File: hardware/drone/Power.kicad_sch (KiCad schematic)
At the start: 96 parts, among them Q1 ISP650P06NM, U1 STM32N645I0, U13 LP5907, U16 LMR51635XFDDCR, U18 TPS2121, U3 TPS628303, U4 TPS7A2118PQWDSGRQ1, U5 TPS628303

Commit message: More footprints
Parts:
- removed C97: 10u, symbol Device:C
- added C114: 2.2u, Capacitor_SMD:C_1206_3216Metric, symbol Device:C
- added C125: 100n, Capacitor_SMD:C_0603_1608Metric, symbol Device:C
- added C126: 22u, Capacitor_SMD:CP_Elec_6.3x5.4, symbol Device:C
- added R45: 2R, Resistor_SMD:R_0402_1005Metric, symbol Device:R
- C10, C100, C101, C102, C103, C104, C105, C106, C107, C108, C109, C110, C111, C112, C113, C115, C24, C9, C99: footprint (none) -> Capacitor_SMD:C_0201_0603Metric
- C13, C14, C15, C17, C18, C2, C26, C27, C28, C3, C4, C5, C80, C81, C86, C89, C96: footprint (none) -> Capacitor_SMD:C_0603_1608Metric
- C21, C7, C8: footprint (none) -> Capacitor_SMD:C_0402_1005Metric
- C6: value 220p -> 2.2n; footprint (none) -> Capacitor_SMD:C_0402_1005Metric
- C85, C95: footprint (none) -> Capacitor_SMD:C_1206_3216Metric
- C87, C88: footprint (none) -> Capacitor_SMD:C_1812_4532Metric
- C98: value 100n -> 1u; footprint (none) -> Capacitor_SMD:C_0402_1005Metric
- D1: value BZX38450-B10 -> MM3Z10
- F1: footprint (none) -> Fuse:Fuse_2920_7451Metric
- FB1, R15, R16: footprint (none) -> Resistor_SMD:R_0603_1608Metric
- FB2, R1, R11, R12, R17, R18, R19, R2, R20, R21, R22, R23, R3, R4: footprint (none) -> Resistor_SMD:R_0402_1005Metric
- R24: value 100k -> 22k; footprint (none) -> Resistor_SMD:R_0603_1608Metric
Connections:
- net GND: now also C114.2, C125.2, C126.2
- net VBAT: now also C114.1, C125.1, C126.1; no longer D2.2 (A2)
- net at L1.2, U1.G1 (VLXSMPS), U1.G2 (VLXSMPS)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: now also R45.2; no longer C6.2
- net at F1.2, Q1.1 (D): now also D2.2 (A2)
- new net: C6.2, R45.1
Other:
- note added: "RVT1H220M0605 C27783"
- note added: "VDDSMPS pins"
- moved on the sheet: C6, C85, C86, C87, C88, C89, C95, C96, C98, D1, D2, F1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

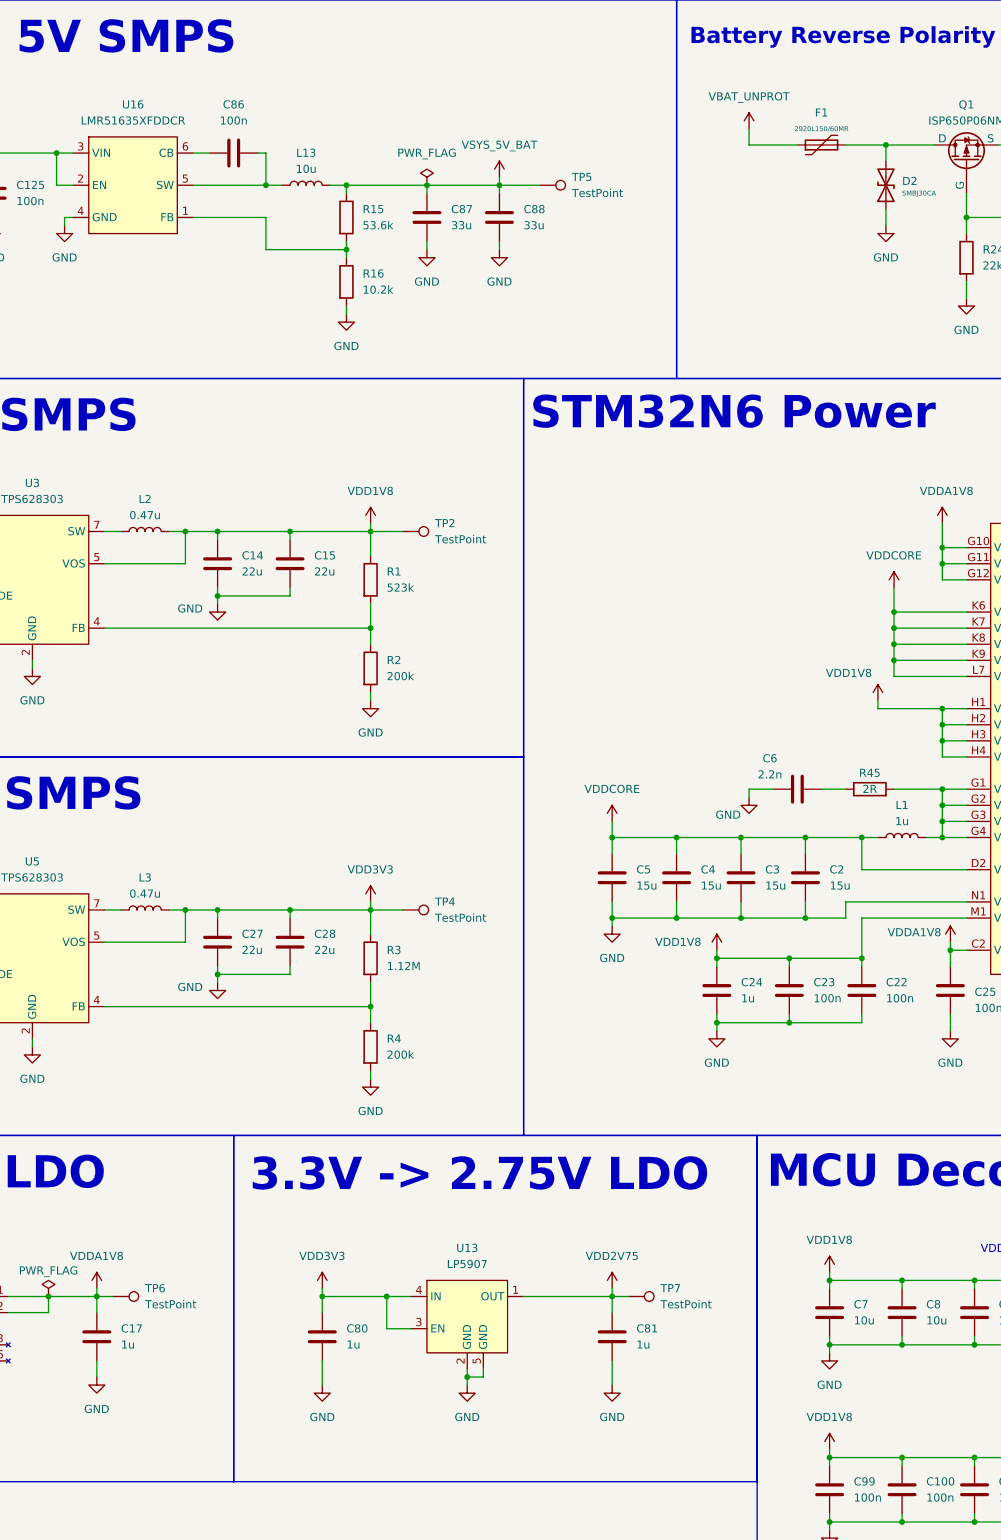
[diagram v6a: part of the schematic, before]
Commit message: Completed footprint assignments
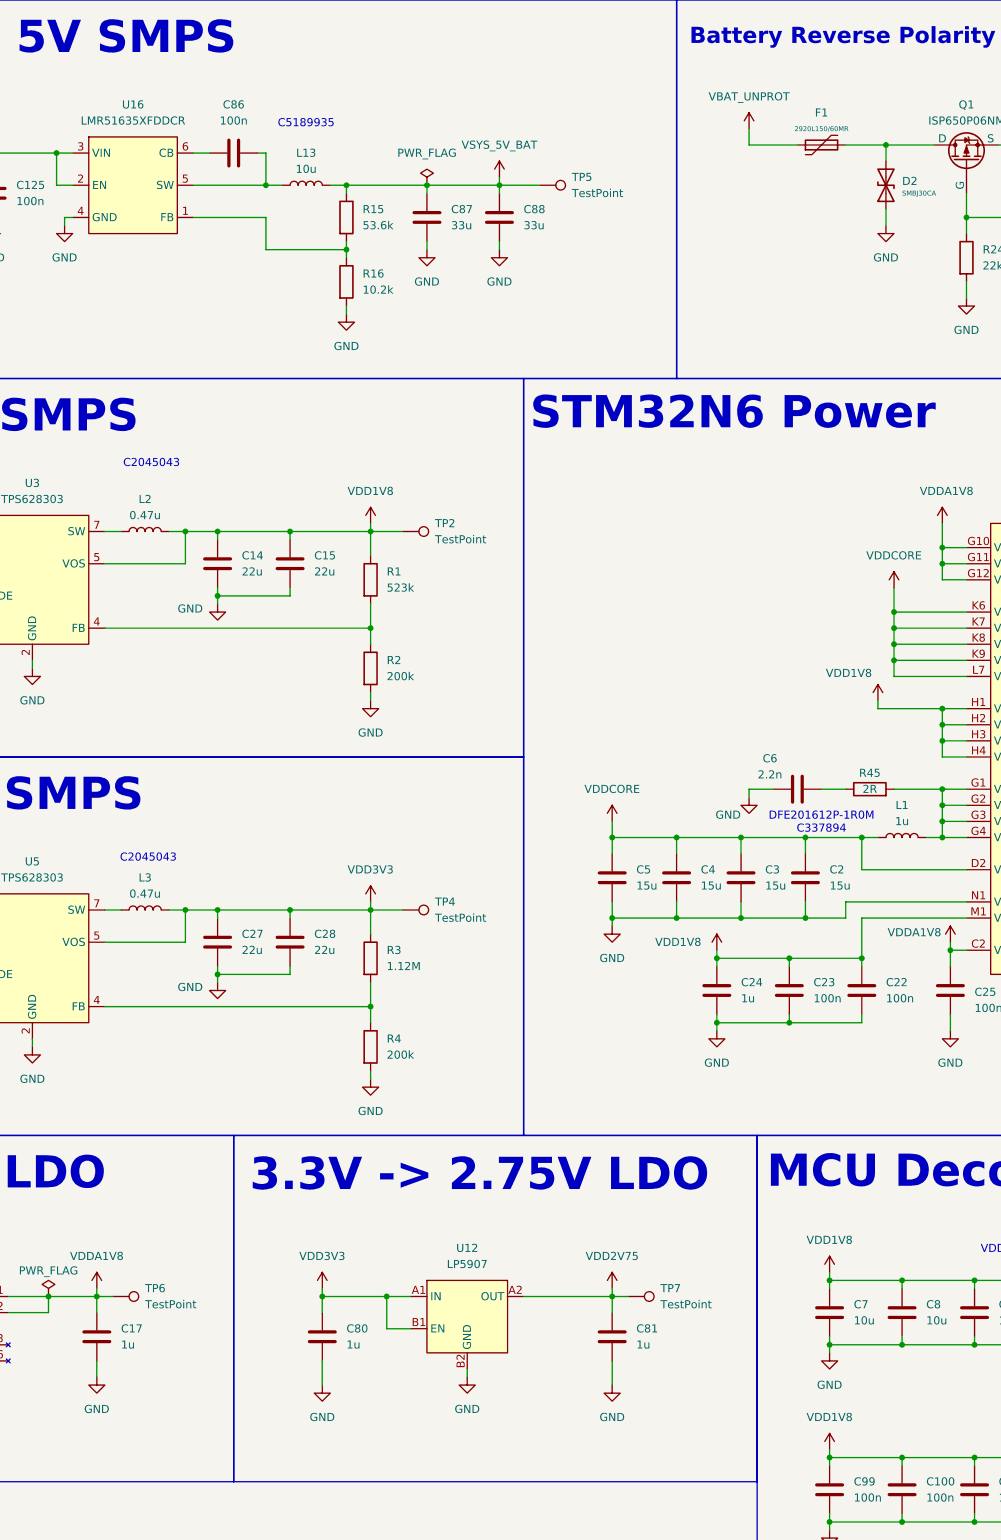
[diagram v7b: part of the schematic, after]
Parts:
- removed U13: LP5907, LP5907A28YKMR:BGA4C35P2X2_64X64X50, symbol SoftDrone:LM5907
- added U12: LP5907, LP5907A28YKMR:BGA4C35P2X2_64X64X50, symbol SoftDrone:LP5907
- D1: footprint (none) -> Diode_SMD:D_SOD-323
- D2: footprint (none) -> Diode_SMD:D_SMB
- L1: footprint (none) -> SoftDroneLibrary:CVH201610A-2R2M
- L13: footprint (none) -> SoftDroneLibrary:CYA0650-10UH
- L2, L3: footprint (none) -> SoftDroneLibrary:TFM201610ALC-R47MTAA
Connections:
- net GND: now also U12.B2 (GND)
- net VDD2V75: now also U12.A2 (OUT)
- net VDD3V3: now also U12.A1 (IN), U12.B1 (EN)
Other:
- note added: "C2045043"
- note added: "C5189935"
- note added: "DFE201612P-1R0M C337894"
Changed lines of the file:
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@@
 		)
 	)
+	(text "DFE201612P-1R0M\nC337894"
+		(exclude_from_sim no)
+		(at 208.28 166.624 0)
+		(effects
+			(font
+				(size 1.27 1.27)
+			)
+		)
+	)
 	(text "RVT1H220M0605\nC27783"
 		(exclude_from_sim no)
@@
 		)
 	)
+	(text "C2045043"
+		(exclude_from_sim no)
+		(at 102.108 172.212 0)
+		(effects
+			(font
+				(size 1.27 1.27)
+			)
+		)
+	)
 	(text "5V Power Mux"
 		(exclude_from_sim no)
@@
 		)
 	)
+	(text "C2045043"
+		(exclude_from_sim no)
+		(at 102.616 109.982 0)
+		(effects
+			(font
+				(size 1.27 1.27)
+			)
+		)
+	)
+	(text "C5189935"
+		(exclude_from_sim no)
+		(at 127 56.388 0)
+		(effects
+			(font
+				(size 1.27 1.27)
+			)
+		)
+	)
 	(text "STM32N6 Power"
 		(exclude_from_sim no)
@@
 	)
 	(junction
-		(at 152.4 254)
-		(diameter 0)
-		(color 0 0 0 0)
-	)
-	(junction
 		(at 243.84 266.7)
 		(diameter 0)
@@
 	(wire
 		(pts
-			(xy 152.4 254) (xy 152.4 252.73)
-		)
-		(stroke
-			(width 0)
-			(type default)
-		)
-	)
-	(wire
-		(pts
 			(xy 205.74 168.91) (xy 205.74 171.45)
 		)
@@
 	(wire
 		(pts
-			(xy 154.94 252.73) (xy 154.94 254)
-		)
-		(stroke
-			(width 0)
-			(type default)
-		)
-	)
-	(wire
-		(pts
 			(xy 217.17 168.91) (xy 214.63 168.91)
 		)
@@
 	(wire
 		(pts
-			(xy 154.94 254) (xy 152.4 254)
-		)
-		(stroke
-			(width 0)
-			(type default)
-		)
-	)
-	(wire
-		(pts
 			(xy 95.25 185.42) (xy 107.95 185.42)
 		)
@@
 	(wire
 		(pts
-			(xy 152.4 254) (xy 152.4 255.27)
+			(xy 152.4 252.73) (xy 152.4 254)
 		)
 		(stroke
@@
 	)
 	(symbol
+		(lib_id "SoftDrone:LP5907")
+		(at 152.4 245.11 0)
+		(unit 1)
+		(body_style 1)
+		(exclude_from_sim no)
+		(in_bom yes)
+		(on_board yes)
+		(in_pos_files yes)
+		(dnp no)
+		(fields_autoplaced yes)
+		(property "Reference" "U12"
+			(at 152.4 233.68 0)
+			(show_name no)
+			(do_not_autoplace no)
+			(effects
+				(font
+					(size 1.27 1.27)
+				)
+			)
+		)
+		(property "Value" "LP5907"
+			(at 152.4 236.22 0)
+			(show_name no)
+			(do_not_autoplace no)
+			(effects
+				(font
+					(size 1.27 1.27)
+				)
+			)
+		)
+		(property "Footprint" "LP5907A28YKMR:BGA4C35P2X2_64X64X50"
+			(at 152.4 245.11 0)
+			(hide yes)
+			(show_name no)
+			(do_not_autoplace no)
+			(effects
+				(font
+					(size 1.27 1.27)
+				)
+			)
+		)
+		(property "Datasheet" ""
+			(at 152.4 245.11 0)
+			(hide yes)
+			(show_name no)
+			(do_not_autoplace no)
+			(effects
+				(font
+					(size 1.27 1.27)
+				)
+			)
+		)
+		(property "Description" ""
+			(at 152.4 245.11 0)
+			(hide yes)
+			(show_name no)
+			(do_not_autoplace no)
+			(effects
+				(font
+					(size 1.27 1.27)
+				)
+			)
+		)
+		(pin "B2"
+		)
+		(pin "B1"
+		)
+		(pin "A1"
+		)
+		(pin "A2"
+		)
+		(instances
+			(project "drone"
+				(path "/62c402a6-ed3f-446b-8423-821e9cc6908b/9b1c1f9e-2215-43f5-a9f4-c7f468848b2f"
+					(reference "U12")
+					(unit 1)
+				)
+			)
+		)
+	)
+	(symbol
 		(lib_id "Device:C")
 		(at 220.98 300.99 0)
@@
 			)
 		)
-		(property "Footprint" ""
+		(property "Footprint" "SoftDroneLibrary:CYA0650-10UH"
 			(at 127 66.04 0)
 			(hide yes)
@@
 			)
 		)
-		(property "Footprint" ""
+		(property "Footprint" "SoftDroneLibrary:CVH201610A-2R2M"
 			(at 220.98 168.91 0)
 			(hide yes)
@@
 			)
 		)
-		(property "Footprint" ""
+		(property "Footprint" "SoftDroneLibrary:TFM201610ALC-R47MTAA"
 			(at 101.6 120.65 0)
 			(hide yes)
@@
 	)
 	(symbol
-		(lib_id "SoftDrone:LM5907")
-		(at 152.4 245.11 0)
-		(unit 1)
-		(body_style 1)
-		(exclude_from_sim no)
-		(in_bom yes)
-		(on_board yes)
-		(in_pos_files yes)
-		(dnp no)
-		(fields_autoplaced yes)
-		(property "Reference" "U13"
-			(at 152.4 233.68 0)
-			(show_name no)
-			(do_not_autoplace no)
-			(effects
-				(font
-					(size 1.27 1.27)
-				)
-			)
-		)
-		(property "Value" "LP5907"
-			(at 152.4 236.22 0)
-			(show_name no)
-			(do_not_autoplace no)
-			(effects
-				(font
-					(size 1.27 1.27)
-				)
-			)
-		)
-		(property "Footprint" "LP5907A28YKMR:BGA4C35P2X2_64X64X50"
-			(at 152.4 245.11 0)
-			(hide yes)
-			(show_name no)
-			(do_not_autoplace no)
-			(effects
-				(font
-					(size 1.27 1.27)
-				)
-			)
-		)
-		(property "Datasheet" ""
-			(at 152.4 245.11 0)
-			(hide yes)
-			(show_name no)
-			(do_not_autoplace no)
-			(effects
-				(font
-					(size 1.27 1.27)
-				)
-			)
-		)
-		(property "Description" ""
-			(at 152.4 245.11 0)
-			(hide yes)
-			(show_name no)
-			(do_not_autoplace no)
-			(effects
-				(font
-					(size 1.27 1.27)
-				)
-			)
-		)
-		(pin "1"
-		)
-		(pin "4"
-		)
-		(pin "3"
-		)
-		(pin "2"
-		)
-		(pin "5"
-		)
-		(instances
-			(project "drone"
-				(path "/62c402a6-ed3f-446b-8423-821e9cc6908b/9b1c1f9e-2215-43f5-a9f4-c7f468848b2f"
-					(reference "U13")
-					(unit 1)
-				)
-			)
-		)
-	)
-	(symbol
 		(lib_id "power:GND")
-		(at 152.4 255.27 0)
+		(at 152.4 254 0)
 		(unit 1)
 		(body_style 1)
@@
 		(fields_autoplaced yes)
 		(property "Reference" "#PWR0104"
-			(at 152.4 261.62 0)
+			(at 152.4 260.35 0)
 			(hide yes)
 			(show_name no)
@@
 		)
 		(property "Value" "GND"
-			(at 152.4 260.35 0)
+			(at 152.4 259.08 0)
 			(show_name no)
 			(do_not_autoplace no)
@@
 		)
 		(property "Footprint" ""
-			(at 152.4 255.27 0)
+			(at 152.4 254 0)
 			(hide yes)
 			(show_name no)
@@
 		)
 		(property "Datasheet" ""
-			(at 152.4 255.27 0)
+			(at 152.4 254 0)
 			(hide yes)
 			(show_name no)
@@
 		)
 		(property "Description" "Power symbol creates a global label with name \"GND\" , ground"
-			(at 152.4 255.27 0)
+			(at 152.4 254 0)
 			(hide yes)
 			(show_name no)
@@
 			)
 		)
-		(property "Footprint" ""
+		(property "Footprint" "Diode_SMD:D_SMB"
 			(at 218.44 66.04 0)
 			(hide yes)
@@
 			)
 		)
-		(property "Footprint" ""
+		(property "Footprint" "Diode_SMD:D_SOD-323"
 			(at 242.57 66.04 0)
 			(hide yes)
@@
 			)
 		)
-		(property "Footprint" ""
+		(property "Footprint" "SoftDroneLibrary:TFM201610ALC-R47MTAA"
 			(at 101.6 180.34 0)
 			(hide yes)
